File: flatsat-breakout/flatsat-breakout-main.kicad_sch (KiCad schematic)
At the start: 5 parts, among them J1 Conn_01x40, J2 Conn_01x40, J3 Conn_01x40, J4 Conn_01x27, J5 Conn_02x08_Odd_Even

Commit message: Fixed signal name silkscreen covered by connector footprint
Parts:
- J2, J3: footprint Connector_PinHeader_2.54mm:PinHeader_2x20_P2.54mm_Vertical -> Connector_IDC:IDC-Header_2x20_P2.54mm_Vertical
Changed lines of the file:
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@@
     (property "Reference" "J3" (id 0) (at 106.172 46.99 0))
     (property "Value" "Conn_01x40" (id 1) (at 106.172 49.53 0))
-    (property "Footprint" "Connector_PinHeader_2.54mm:PinHeader_2x20_P2.54mm_Vertical" (id 2) (at 104.14 101.6 0)
+    (property "Footprint" "Connector_IDC:IDC-Header_2x20_P2.54mm_Vertical" (id 2) (at 104.14 101.6 0)
       (effects (font (size 1.27 1.27)) hide)
     )
@@
     (property "Reference" "J2" (id 0) (at 96.012 46.99 0))
     (property "Value" "Conn_01x40" (id 1) (at 96.012 49.53 0))
-    (property "Footprint" "Connector_PinHeader_2.54mm:PinHeader_2x20_P2.54mm_Vertical" (id 2) (at 93.98 101.6 0)
+    (property "Footprint" "Connector_IDC:IDC-Header_2x20_P2.54mm_Vertical" (id 2) (at 93.98 101.6 0)
       (effects (font (size 1.27 1.27)) hide)
     )
@@
     )
     (path "/dc1bbcc9-ee51-40f1-8280-08a3863581c3"
-      (reference "J2") (unit 1) (value "Conn_01x40") (footprint "Connector_PinHeader_2.54mm:PinHeader_2x20_P2.54mm_Vertical")
+      (reference "J2") (unit 1) (value "Conn_01x40") (footprint "Connector_IDC:IDC-Header_2x20_P2.54mm_Vertical")
     )
     (path "/3376b2e0-8f3f-4d46-b094-eca914ece75a"
-      (reference "J3") (unit 1) (value "Conn_01x40") (footprint "Connector_PinHeader_2.54mm:PinHeader_2x20_P2.54mm_Vertical")
+      (reference "J3") (unit 1) (value "Conn_01x40") (footprint "Connector_IDC:IDC-Header_2x20_P2.54mm_Vertical")
     )
     (path "/83f85e22-fe20-4ffa-b437-52ec5beed00a"

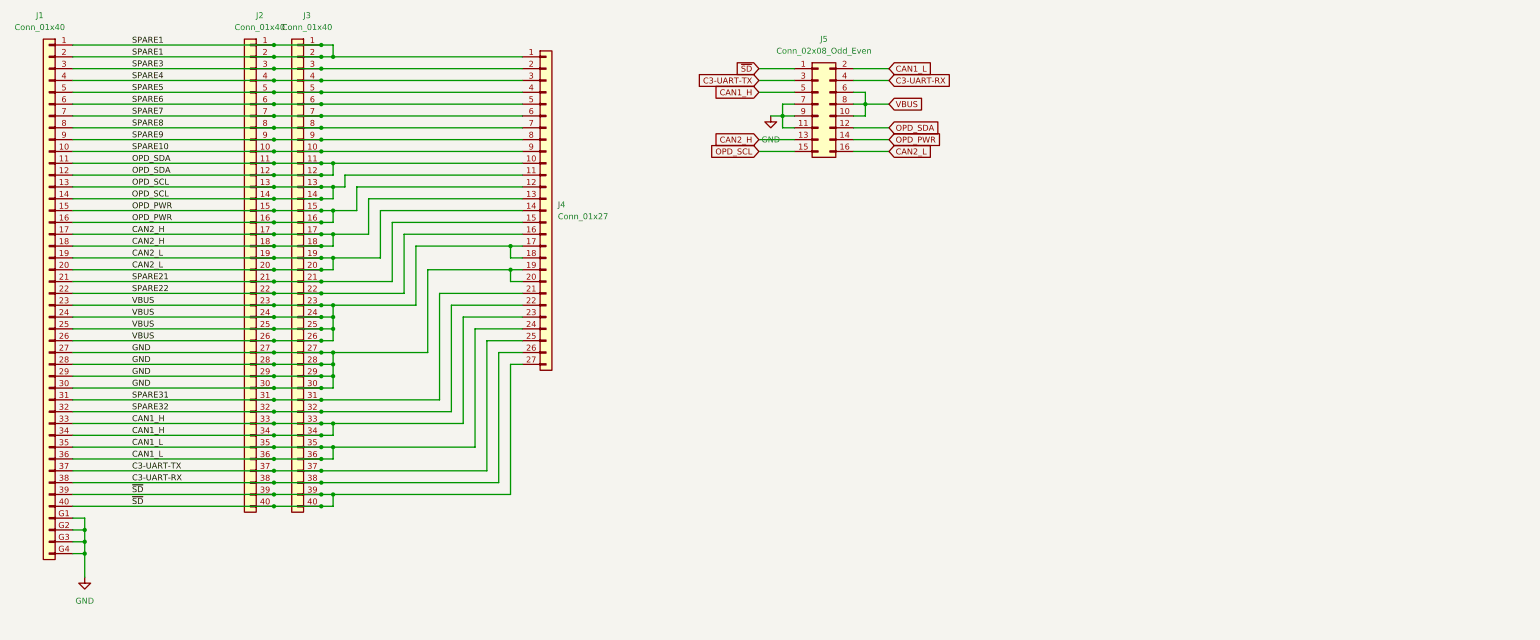
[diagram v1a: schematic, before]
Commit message: Updated to latest KiCAD, added BOM info to parts, updated 3D model, cleaned up silkscreen, rounded board edges.
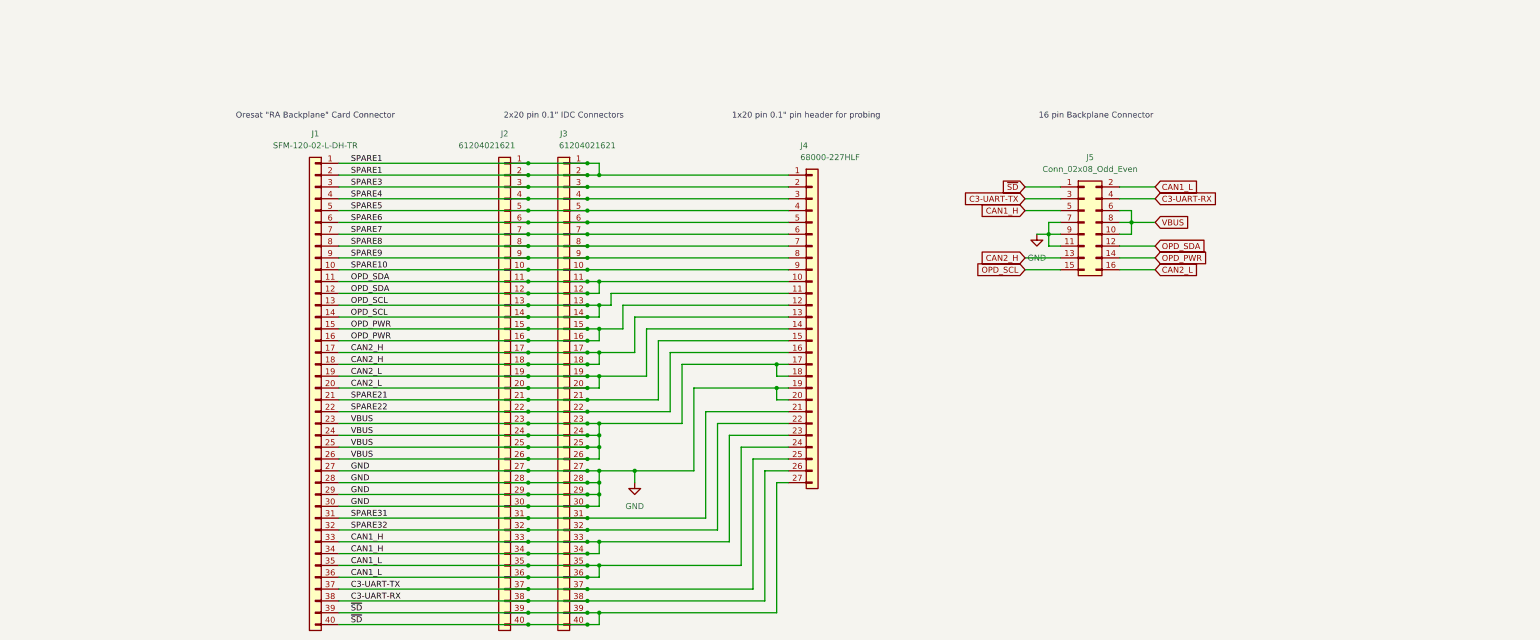
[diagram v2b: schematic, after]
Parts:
- J1: value Conn_01x40 -> SFM-120-02-L-DH-TR; footprint J-SAMTEC-SFM-120-02-X-DH:SFM-120-02-X-DH -> oresat-connectors:SFM-120-02-X-DH; DIS (none) -> DigiKey; DPN (none) -> SAM14509CT-ND; MFR (none) -> Samtec; MPN (none) -> SFM-120-02-L-DH-TR
- J2, J3: value Conn_01x40 -> 61204021621; footprint Connector_IDC:IDC-Header_2x20_P2.54mm_Vertical -> (none); DIS (none) -> DigiKey; DPN (none) -> 732-5401-ND; MFR (none) -> Wurth; MPN (none) -> 61204021621
- J4: value Conn_01x27 -> 68000-227HLF; DIS (none) -> DigiKey; DPN (none) -> 68000-227HLF-ND; MFR (none) -> Amphenol; MPN (none) -> 68000-227HLF
- J5: DIS (none) -> DigiKey; DPN (none) -> 732-2095-ND; MFR (none) -> Wurth; MPN (none) -> 61201621621
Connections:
- net GND: no longer J1.G1 (Pin_41), J1.G2 (Pin_42), J1.G3 (Pin_43), J1.G4 (Pin_44)
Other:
- note added: "16 pin Backplane Connector"
- note added: "1x20 pin 0.1" pin header for probing"
- note added: "2x20 pin 0.1" IDC Connectors"
- note added: "Oresat "RA Backplane" Card Connector"
- title: (none) -> OreSat FlatSat Card Connector
- moved on the sheet: J2, J3, J4, J5

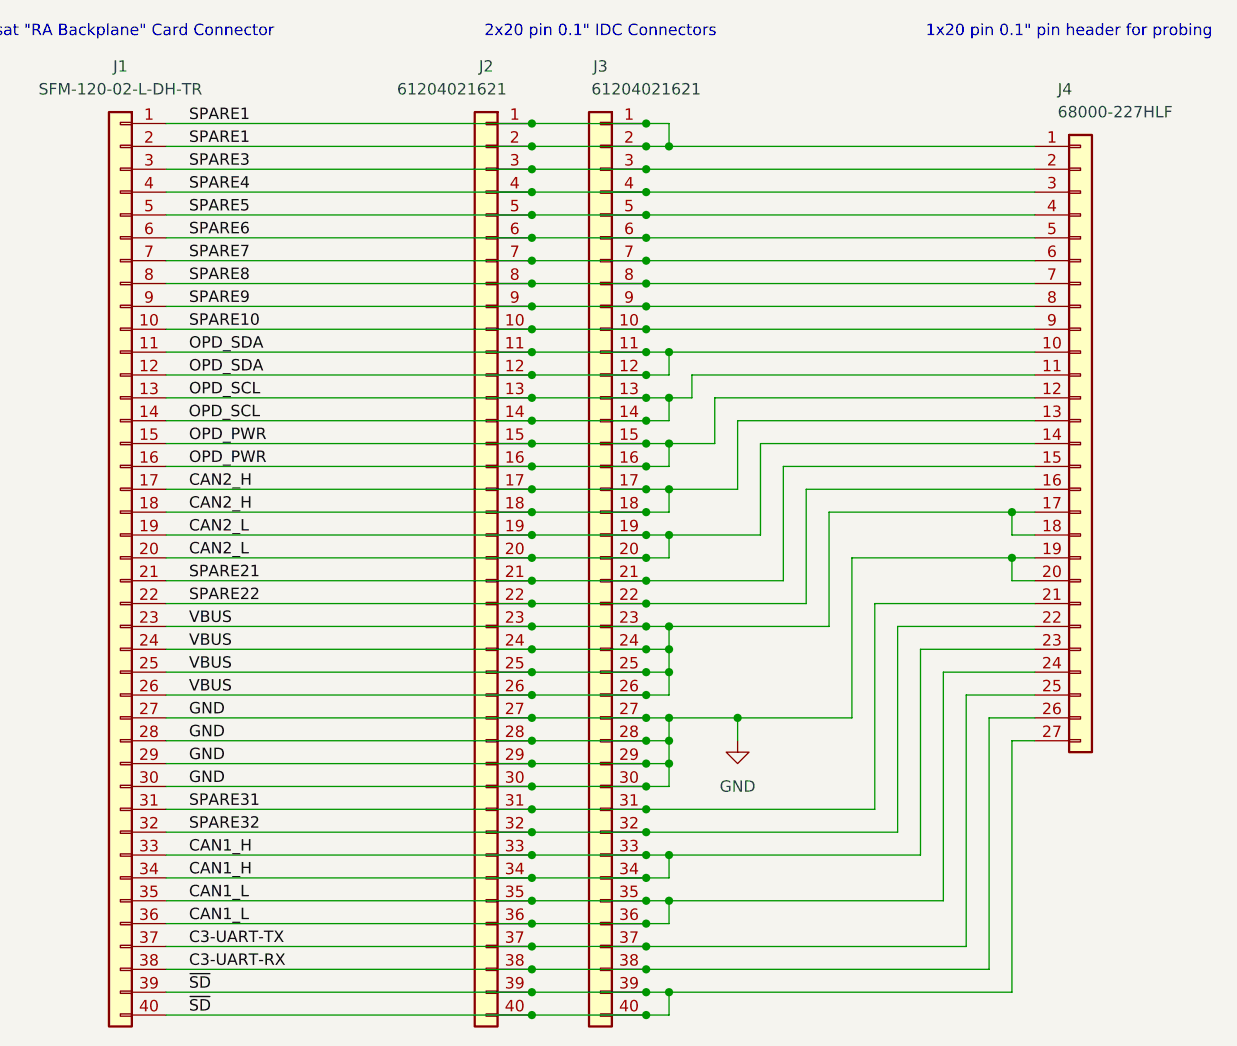
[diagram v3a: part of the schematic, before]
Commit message: Added local variables to make connections clear, Modifed connector so that it matches OreSat1 backplane connector
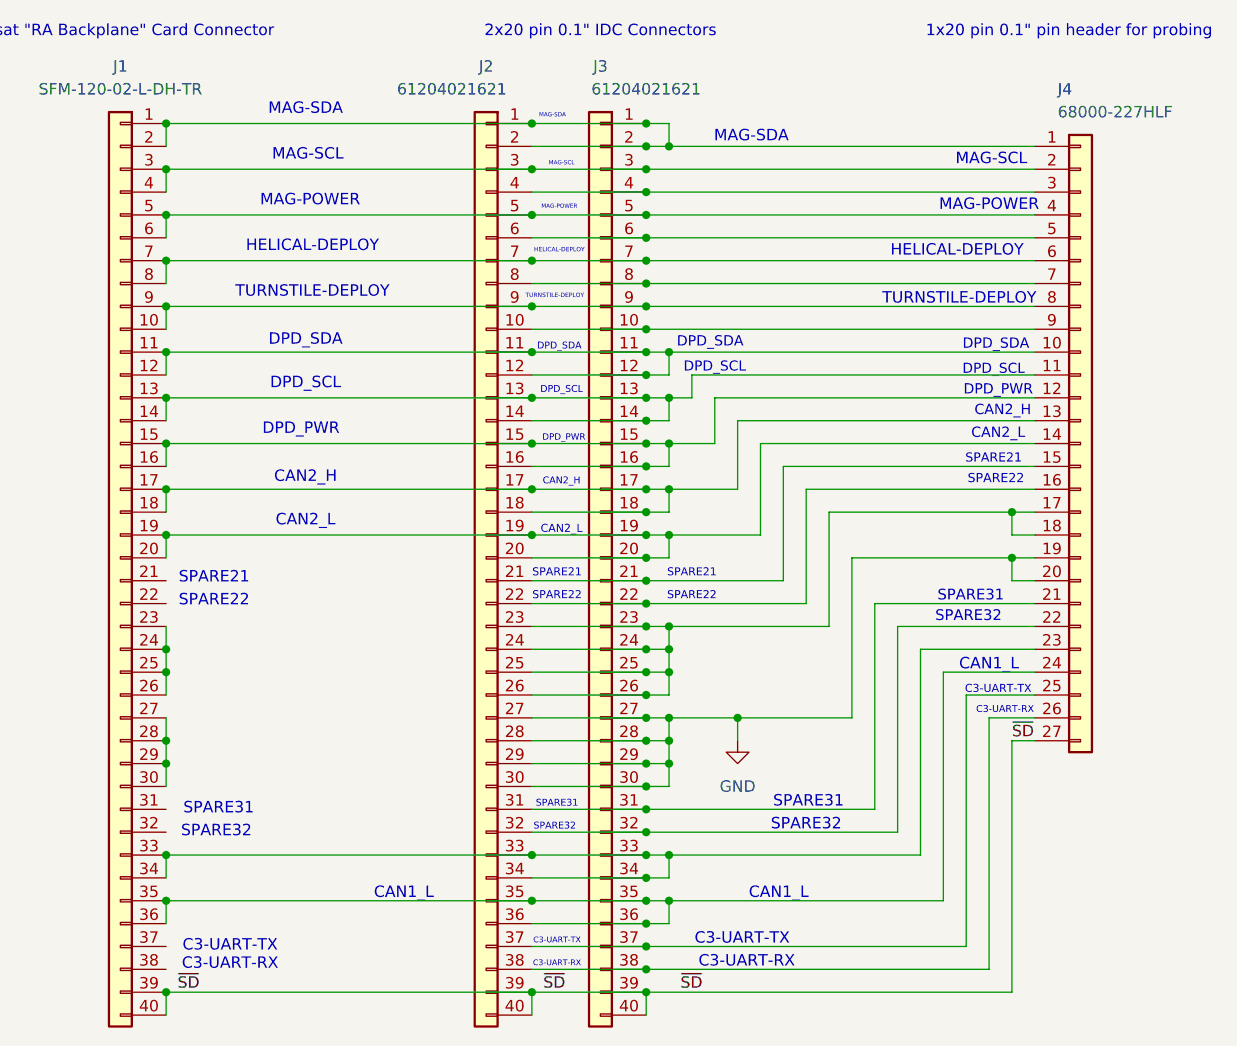
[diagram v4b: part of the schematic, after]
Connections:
- net C3-UART-RX: no longer J1.38 (Pin_38), J2.38 (Pin_38), J3.38 (Pin_38), J4.26 (Pin_26)
- net C3-UART-TX: no longer J1.37 (Pin_37), J2.37 (Pin_37), J3.37 (Pin_37), J4.25 (Pin_25)
- net CAN1_H: no longer J1.33 (Pin_33), J1.34 (Pin_34), J2.33 (Pin_33), J2.34 (Pin_34), J3.33 (Pin_33), J3.34 (Pin_34), J4.23 (Pin_23)
- net CAN1_L: no longer J1.35 (Pin_35), J1.36 (Pin_36), J2.35 (Pin_35), J2.36 (Pin_36), J3.35 (Pin_35), J3.36 (Pin_36), J4.24 (Pin_24)
- net CAN2_H: no longer J1.17 (Pin_17), J1.18 (Pin_18), J2.17 (Pin_17), J2.18 (Pin_18), J3.17 (Pin_17), J3.18 (Pin_18), J4.13 (Pin_13)
- net CAN2_L: no longer J1.19 (Pin_19), J1.20 (Pin_20), J2.19 (Pin_19), J2.20 (Pin_20), J3.19 (Pin_19), J3.20 (Pin_20), J4.14 (Pin_14)
- net GND: no longer J1.27 (Pin_27), J1.28 (Pin_28), J1.29 (Pin_29), J1.30 (Pin_30)
- net OPD_PWR: no longer J1.15 (Pin_15), J1.16 (Pin_16), J2.15 (Pin_15), J2.16 (Pin_16), J3.15 (Pin_15), J3.16 (Pin_16), J4.12 (Pin_12)
- net OPD_SCL: no longer J1.13 (Pin_13), J1.14 (Pin_14), J2.13 (Pin_13), J2.14 (Pin_14), J3.13 (Pin_13), J3.14 (Pin_14), J4.11 (Pin_11)
- net OPD_SDA: no longer J1.11 (Pin_11), J1.12 (Pin_12), J2.11 (Pin_11), J2.12 (Pin_12), J3.11 (Pin_11), J3.12 (Pin_12), J4.10 (Pin_10)
- net VBUS: no longer J1.23 (Pin_23), J1.24 (Pin_24), J1.25 (Pin_25), J1.26 (Pin_26), J2.23 (Pin_23), J2.24 (Pin_24), J2.25 (Pin_25), J2.26 (Pin_26), J3.23 (Pin_23), J3.24 (Pin_24), J3.25 (Pin_25), J3.26 (Pin_26), J4.17 (Pin_17), J4.18 (Pin_18)
- net SPARE1: no longer names the net of J1.1 (Pin_1), J1.2 (Pin_2), J2.1 (Pin_1), J2.2 (Pin_2), J3.1 (Pin_1), J3.2 (Pin_2), J4.1 (Pin_1)
- net SPARE10: no longer names the net of J2.10 (Pin_10), J3.10 (Pin_10), J4.9 (Pin_9)
- net SPARE10: no longer J1.10 (Pin_10)
- net SPARE21: no longer names the net of J2.21 (Pin_21), J3.21 (Pin_21), J4.15 (Pin_15)
- net SPARE21: no longer J1.21 (Pin_21)
- net SPARE22: no longer names the net of J2.22 (Pin_22), J3.22 (Pin_22), J4.16 (Pin_16)
- net SPARE22: no longer J1.22 (Pin_22)
- net SPARE3: no longer names the net of J1.3 (Pin_3), J2.3 (Pin_3), J3.3 (Pin_3), J4.2 (Pin_2)
- net SPARE3: now also J1.4 (Pin_4)
- net SPARE31: no longer names the net of J2.31 (Pin_31), J3.31 (Pin_31), J4.21 (Pin_21)
- net SPARE31: no longer J1.31 (Pin_31)
- net SPARE32: no longer names the net of J2.32 (Pin_32), J3.32 (Pin_32), J4.22 (Pin_22)
- net SPARE32: no longer J1.32 (Pin_32)
- net SPARE4: no longer names the net of J2.4 (Pin_4), J3.4 (Pin_4), J4.3 (Pin_3)
- net SPARE4: no longer J1.4 (Pin_4)
- net SPARE5: no longer names the net of J1.5 (Pin_5), J2.5 (Pin_5), J3.5 (Pin_5), J4.4 (Pin_4)
- net SPARE5: now also J1.6 (Pin_6)
- net SPARE6: no longer names the net of J2.6 (Pin_6), J3.6 (Pin_6), J4.5 (Pin_5)
- net SPARE6: no longer J1.6 (Pin_6)
- net SPARE7: no longer names the net of J1.7 (Pin_7), J2.7 (Pin_7), J3.7 (Pin_7), J4.6 (Pin_6)
- net SPARE7: now also J1.8 (Pin_8)
- net SPARE8: no longer names the net of J2.8 (Pin_8), J3.8 (Pin_8), J4.7 (Pin_7)
- net SPARE8: no longer J1.8 (Pin_8)
- net SPARE9: no longer names the net of J1.9 (Pin_9), J2.9 (Pin_9), J3.9 (Pin_9), J4.8 (Pin_8)
- net SPARE9: now also J1.10 (Pin_10)
- new net: J1.11 (Pin_11), J1.12 (Pin_12), J2.11 (Pin_11), J2.12 (Pin_12), J3.11 (Pin_11), J3.12 (Pin_12), J4.10 (Pin_10)
- new net: J1.13 (Pin_13), J1.14 (Pin_14), J2.13 (Pin_13), J2.14 (Pin_14), J3.13 (Pin_13), J3.14 (Pin_14), J4.11 (Pin_11)
- new net: J1.15 (Pin_15), J1.16 (Pin_16), J2.15 (Pin_15), J2.16 (Pin_16), J3.15 (Pin_15), J3.16 (Pin_16), J4.12 (Pin_12)
- new net: J1.17 (Pin_17), J1.18 (Pin_18), J2.17 (Pin_17), J2.18 (Pin_18), J3.17 (Pin_17), J3.18 (Pin_18), J4.13 (Pin_13)
- new net: J1.19 (Pin_19), J1.20 (Pin_20), J2.19 (Pin_19), J2.20 (Pin_20), J3.19 (Pin_19), J3.20 (Pin_20), J4.14 (Pin_14)
- new net: J2.23 (Pin_23), J2.24 (Pin_24), J2.25 (Pin_25), J2.26 (Pin_26), J3.23 (Pin_23), J3.24 (Pin_24), J3.25 (Pin_25), J3.26 (Pin_26), J4.17 (Pin_17), J4.18 (Pin_18)
- new net: J1.33 (Pin_33), J1.34 (Pin_34), J2.33 (Pin_33), J2.34 (Pin_34), J3.33 (Pin_33), J3.34 (Pin_34), J4.23 (Pin_23)
- new net: J1.35 (Pin_35), J1.36 (Pin_36), J2.35 (Pin_35), J2.36 (Pin_36), J3.35 (Pin_35), J3.36 (Pin_36), J4.24 (Pin_24)
- new net: J2.37 (Pin_37), J3.37 (Pin_37), J4.25 (Pin_25)
- new net: J2.38 (Pin_38), J3.38 (Pin_38), J4.26 (Pin_26)
- new net: J1.23 (Pin_23), J1.24 (Pin_24), J1.25 (Pin_25), J1.26 (Pin_26)
- new net: J1.27 (Pin_27), J1.28 (Pin_28), J1.29 (Pin_29), J1.30 (Pin_30)
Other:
- note added: "C3-UART-RX"
- note added: "C3-UART-TX"
- note added: "CAN1_L"
- note added: "CAN2_H"
- note added: "CAN2_L"
- note added: "DPD_PWR"
- note added: "DPD_SCL"
- note added: "DPD_SDA"
- note added: "HELICAL-DEPLOY"
- note added: "MAG-POWER"
- note added: "MAG-SCL"
- note added: "MAG-SDA"
- note added: "SPARE21"
- note added: "SPARE22"
- note added: "SPARE31"
- note added: "SPARE32"
- note added: "TURNSTILE-DEPLOY"

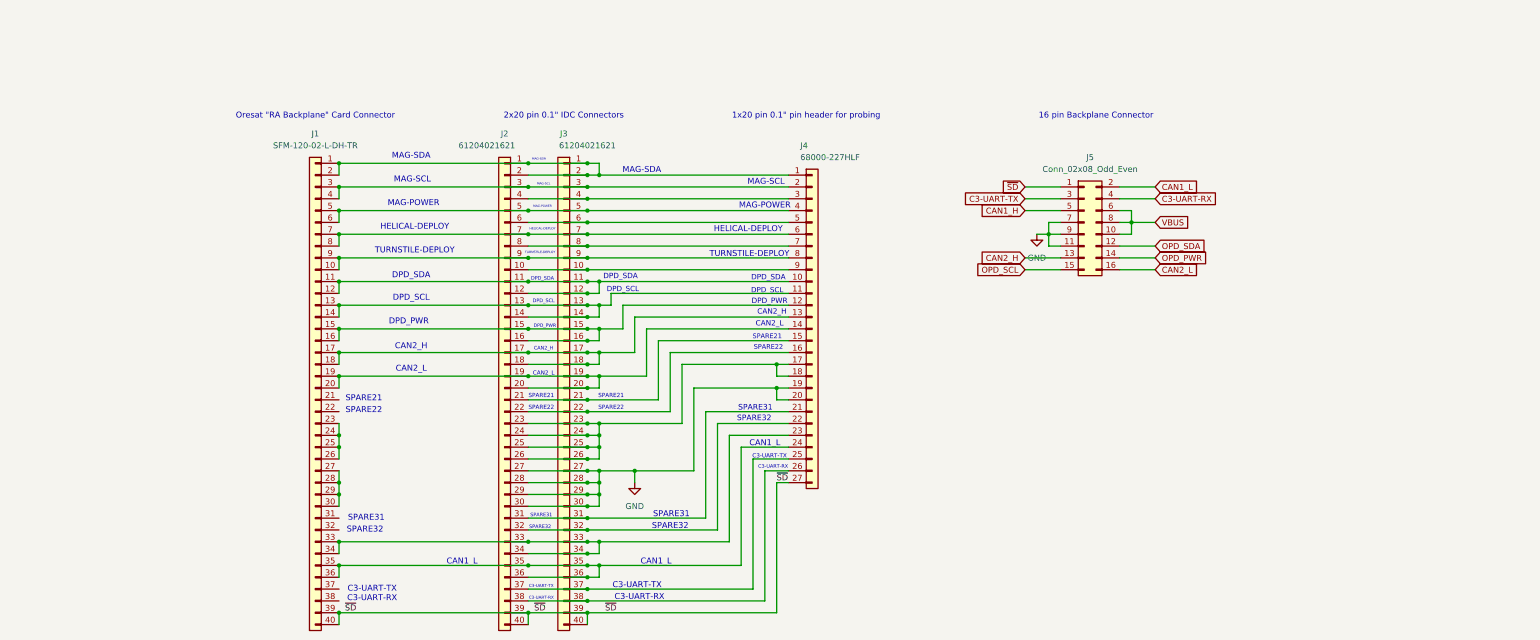
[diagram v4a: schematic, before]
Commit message: Added power and ground labels, added labels on each wire to ensure connections are clear.
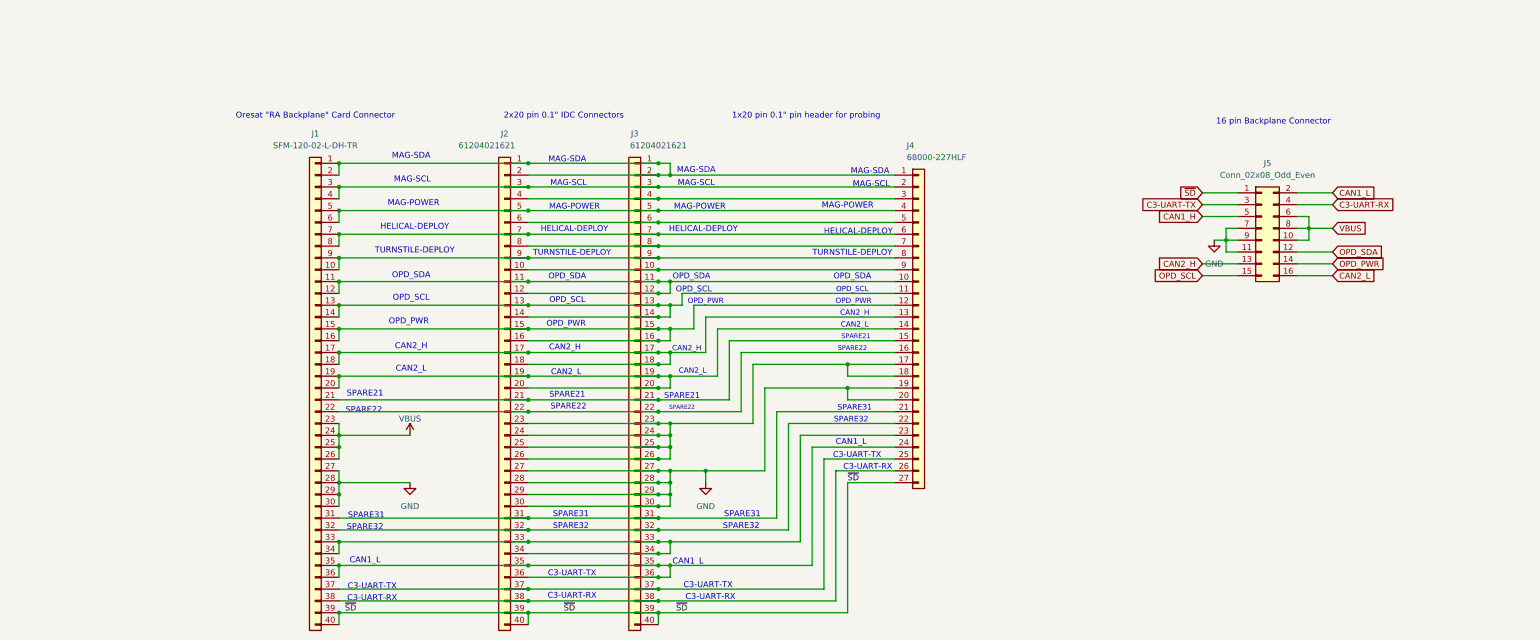
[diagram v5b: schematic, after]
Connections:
- net GND: now also J1.27 (Pin_27), J1.28 (Pin_28), J1.29 (Pin_29), J1.30 (Pin_30)
- net VBUS: now also J1.23 (Pin_23), J1.24 (Pin_24), J1.25 (Pin_25), J1.26 (Pin_26)
- net at J2.21 (Pin_21), J3.21 (Pin_21), J4.15 (Pin_15): now also J1.21 (Pin_21)
- net at J2.22 (Pin_22), J3.22 (Pin_22), J4.16 (Pin_16): now also J1.22 (Pin_22)
- net at J2.31 (Pin_31), J3.31 (Pin_31), J4.21 (Pin_21): now also J1.31 (Pin_31)
- net at J2.32 (Pin_32), J3.32 (Pin_32), J4.22 (Pin_22): now also J1.32 (Pin_32)
- net at J2.37 (Pin_37), J3.37 (Pin_37), J4.25 (Pin_25): now also J1.37 (Pin_37)
- net at J2.38 (Pin_38), J3.38 (Pin_38), J4.26 (Pin_26): now also J1.38 (Pin_38)
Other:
- note added: "OPD_PWR"
- note added: "OPD_SCL"
- note added: "OPD_SDA"
- note removed: "DPD_PWR"
- note removed: "DPD_SCL"
- note removed: "DPD_SDA"
- moved on the sheet: J3, J4, J5
